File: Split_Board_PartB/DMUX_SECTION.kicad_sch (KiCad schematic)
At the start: 32 parts, among them J2 Conn_01x28, J3 Conn_01x28, U22 CD74HC4051PWT, U25 OPA187IDBVR, U30 CD74HC595SM96

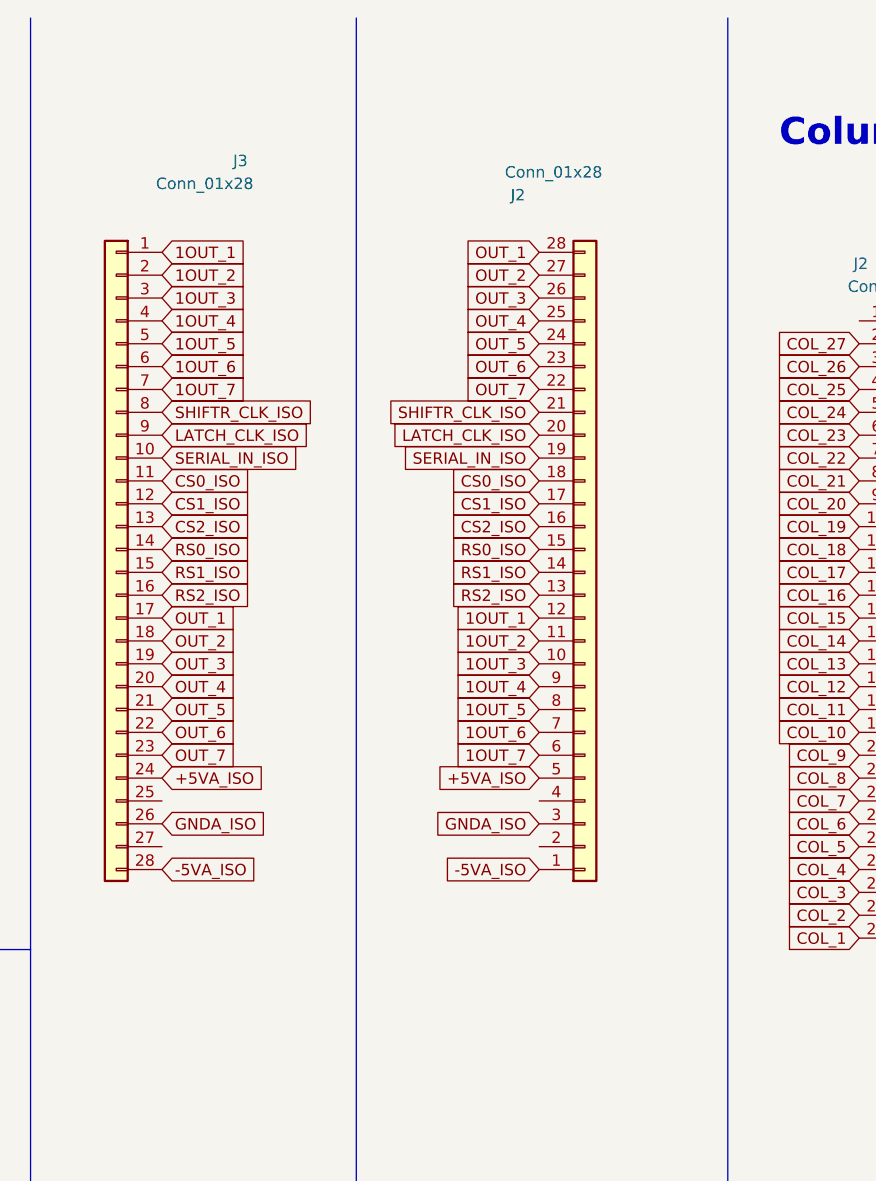
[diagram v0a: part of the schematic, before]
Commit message: led indicator added in part B
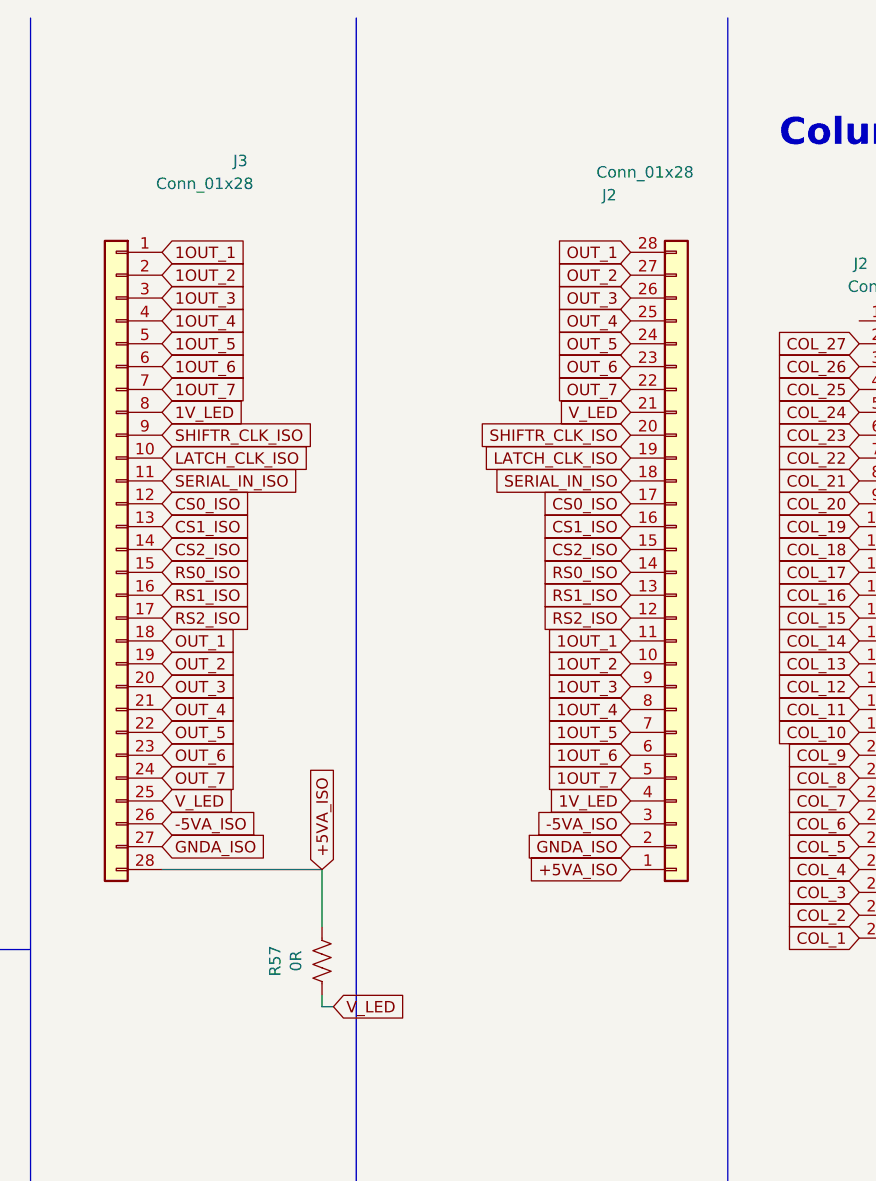
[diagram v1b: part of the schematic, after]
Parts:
- added R57: 0R, Resistor_SMD:R_0805_2012Metric_Pad1.20x1.40mm_HandSolder, symbol Device:R_US
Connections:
- net +5VA_ISO: now also J2.1 (Pin_1), J3.28 (Pin_28), R57.1; no longer J2.5 (Pin_5), J3.24 (Pin_24)
- net -5VA_ISO: now also J2.3 (Pin_3), J3.26 (Pin_26); no longer J2.1 (Pin_1), J3.28 (Pin_28)
- net 1OUT_1: now also J2.11 (Pin_11); no longer J2.12 (Pin_12)
- net 1OUT_2: now also J2.10 (Pin_10); no longer J2.11 (Pin_11)
- net 1OUT_3: now also J2.9 (Pin_9); no longer J2.10 (Pin_10)
- net 1OUT_4: now also J2.8 (Pin_8); no longer J2.9 (Pin_9)
- net 1OUT_5: now also J2.7 (Pin_7); no longer J2.8 (Pin_8)
- net 1OUT_6: now also J2.6 (Pin_6); no longer J2.7 (Pin_7)
- net 1OUT_7: now also J2.5 (Pin_5); no longer J2.6 (Pin_6)
- net CS0_ISO: now also J2.17 (Pin_17), J3.12 (Pin_12); no longer J2.18 (Pin_18), J3.11 (Pin_11)
- net CS1_ISO: now also J2.16 (Pin_16), J3.13 (Pin_13); no longer J2.17 (Pin_17), J3.12 (Pin_12)
- net CS2_ISO: now also J2.15 (Pin_15), J3.14 (Pin_14); no longer J2.16 (Pin_16), J3.13 (Pin_13)
- net GNDA: now also J2.2 (Pin_2), J3.27 (Pin_27); no longer J2.3 (Pin_3), J3.26 (Pin_26)
- net LATCH_CLK_ISO: now also J2.19 (Pin_19), J3.10 (Pin_10); no longer J2.20 (Pin_20), J3.9 (Pin_9)
- net OUT_1: now also J3.18 (Pin_18); no longer J3.17 (Pin_17)
- net OUT_2: now also J3.19 (Pin_19); no longer J3.18 (Pin_18)
- net OUT_3: now also J3.20 (Pin_20); no longer J3.19 (Pin_19)
- net OUT_4: now also J3.21 (Pin_21); no longer J3.20 (Pin_20)
- net OUT_5: now also J3.22 (Pin_22); no longer J3.21 (Pin_21)
- net OUT_6: now also J3.23 (Pin_23); no longer J3.22 (Pin_22)
- net OUT_7: now also J3.24 (Pin_24); no longer J3.23 (Pin_23)
- net RS0_ISO: now also J2.14 (Pin_14), J3.15 (Pin_15); no longer J2.15 (Pin_15), J3.14 (Pin_14)
- net RS1_ISO: now also J2.13 (Pin_13), J3.16 (Pin_16); no longer J2.14 (Pin_14), J3.15 (Pin_15)
- net RS2_ISO: now also J2.12 (Pin_12), J3.17 (Pin_17); no longer J2.13 (Pin_13), J3.16 (Pin_16)
- net SERIAL_IN_ISO: now also J2.18 (Pin_18), J3.11 (Pin_11); no longer J2.19 (Pin_19), J3.10 (Pin_10)
- net SHIFTR_CLK_ISO: now also J2.20 (Pin_20), J3.9 (Pin_9); no longer J2.21 (Pin_21), J3.8 (Pin_8)
- net 1V_LED: now reaches J2.4 (Pin_4)
- net 1V_LED: now also J3.8 (Pin_8)
- net V_LED: now reaches J3.25 (Pin_25)
- net V_LED: now also J2.21 (Pin_21), R57.2
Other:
- moved on the sheet: J2

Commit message: Removed the gerber files of espv5.0
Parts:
- R57: value 0R -> 1K
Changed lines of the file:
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@@
     (stroke (width 0) (type default))
   )
-  (polyline (pts (xy 336.55 12.065) (xy 336.55 252.73))
+  (polyline (pts (xy 347.345 12.065) (xy 347.345 252.73))
     (stroke (width 0) (type default))
   )
@@
       (effects (font (size 1.27 1.27)))
     )
-    (property "Value" "0R" (at 329.8444 116.84 90)
+    (property "Value" "1K" (at 329.8444 116.84 90)
       (effects (font (size 1.27 1.27)))
     )

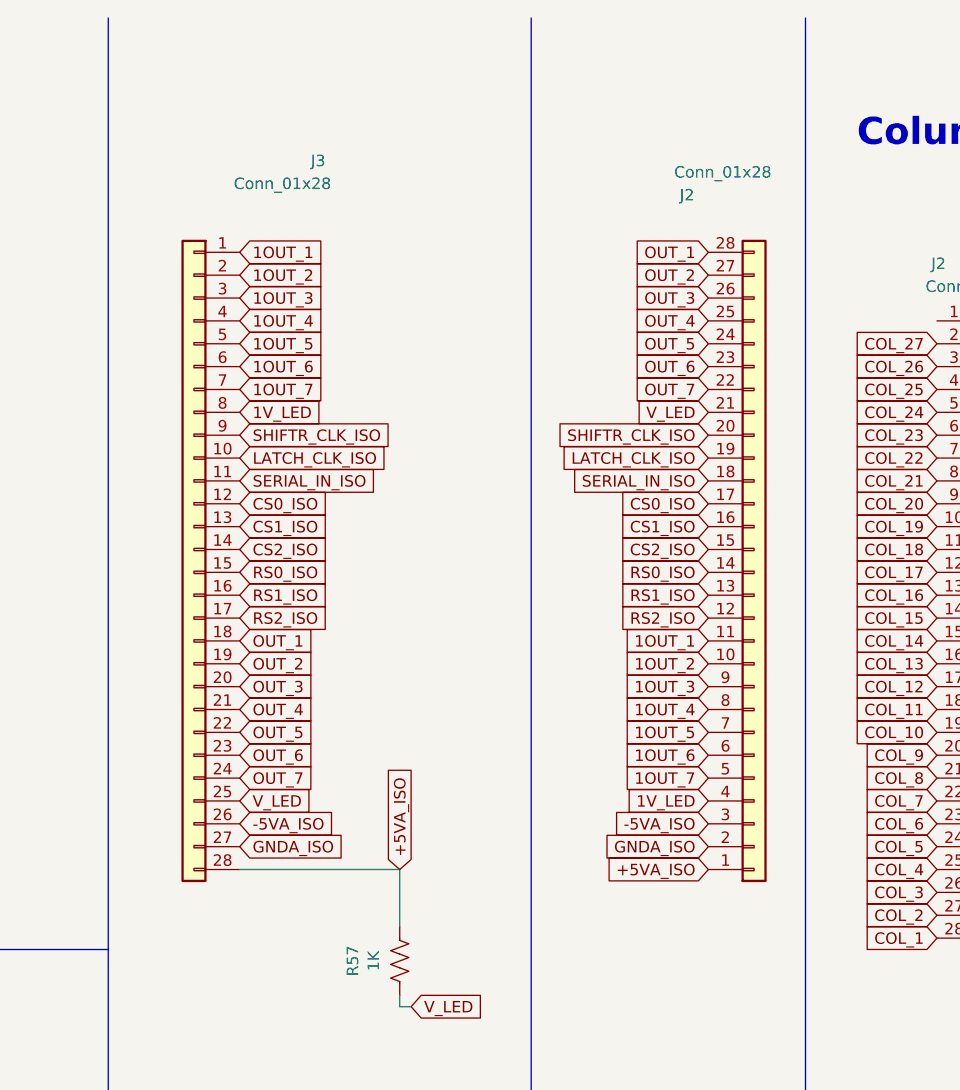
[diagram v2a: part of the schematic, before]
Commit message: added a adapter board in part b and edited the db37 connector in part A
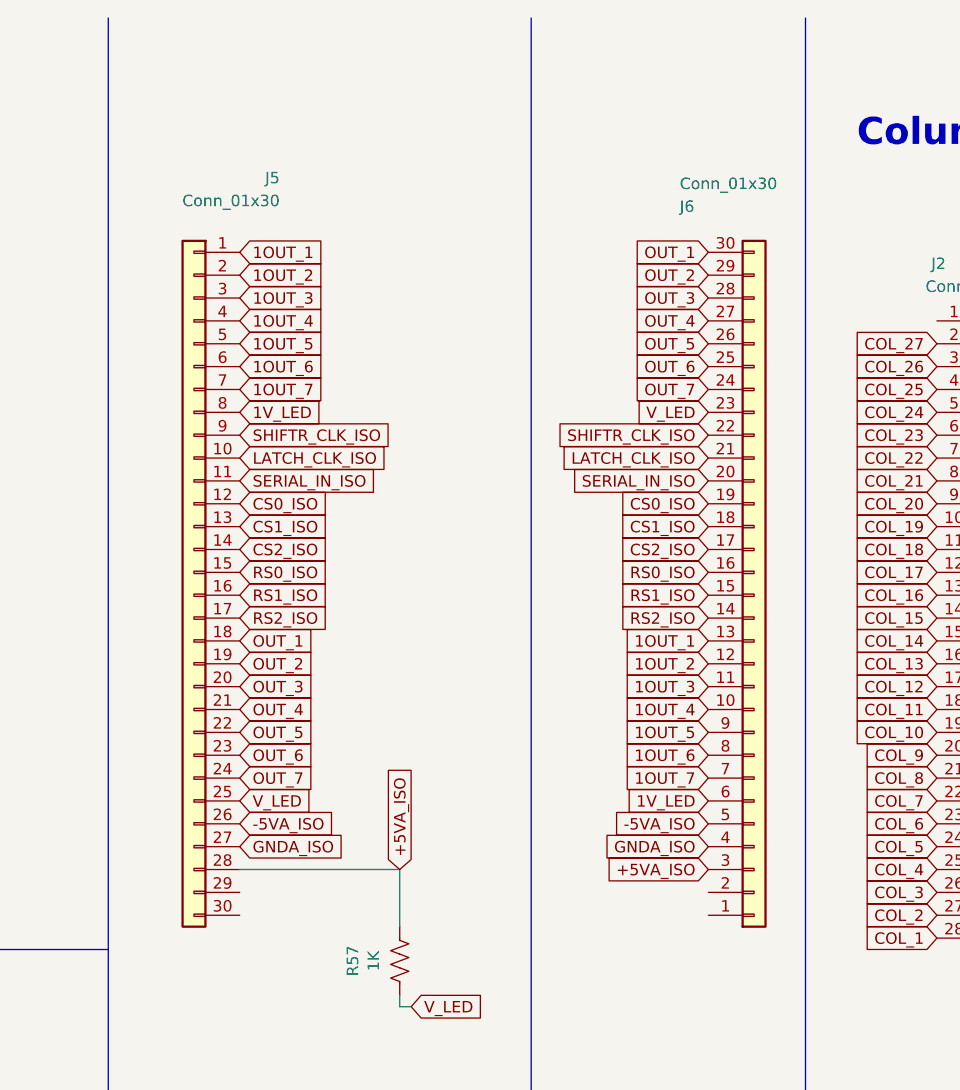
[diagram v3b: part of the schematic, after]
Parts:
- removed J2, J3: Conn_01x28, SamacSys_Parts:522072833, symbol Connector_Generic:Conn_01x28
- added J5, J6: Conn_01x30, symbol Connector_Generic:Conn_01x30
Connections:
- net +5VA_ISO: now also J5.28 (Pin_28), J6.3 (Pin_3)
- net -5VA_ISO: now also J5.26 (Pin_26), J6.5 (Pin_5)
- net 1OUT_1: now also J5.1 (Pin_1), J6.13 (Pin_13)
- net 1OUT_2: now also J5.2 (Pin_2), J6.12 (Pin_12)
- net 1OUT_3: now also J5.3 (Pin_3), J6.11 (Pin_11)
- net 1OUT_4: now also J5.4 (Pin_4), J6.10 (Pin_10)
- net 1OUT_5: now also J5.5 (Pin_5), J6.9 (Pin_9)
- net 1OUT_6: now also J5.6 (Pin_6), J6.8 (Pin_8)
- net 1OUT_7: now also J5.7 (Pin_7), J6.7 (Pin_7)
- net 1V_LED: now also J5.8 (Pin_8), J6.6 (Pin_6)
- net CS0_ISO: now also J5.12 (Pin_12), J6.19 (Pin_19)
- net CS1_ISO: now also J5.13 (Pin_13), J6.18 (Pin_18)
- net CS2_ISO: now also J5.14 (Pin_14), J6.17 (Pin_17)
- net GNDA: now also J5.27 (Pin_27), J6.4 (Pin_4)
- net LATCH_CLK_ISO: now also J5.10 (Pin_10), J6.21 (Pin_21)
- net OUT_1: now also J5.18 (Pin_18), J6.30 (Pin_30)
- net OUT_2: now also J5.19 (Pin_19), J6.29 (Pin_29)
- net OUT_3: now also J5.20 (Pin_20), J6.28 (Pin_28)
- net OUT_4: now also J5.21 (Pin_21), J6.27 (Pin_27)
- net OUT_5: now also J5.22 (Pin_22), J6.26 (Pin_26)
- net OUT_6: now also J5.23 (Pin_23), J6.25 (Pin_25)
- net OUT_7: now also J5.24 (Pin_24), J6.24 (Pin_24)
- net RS0_ISO: now also J5.15 (Pin_15), J6.16 (Pin_16)
- net RS1_ISO: now also J5.16 (Pin_16), J6.15 (Pin_15)
- net RS2_ISO: now also J5.17 (Pin_17), J6.14 (Pin_14)
- net SERIAL_IN_ISO: now also J5.11 (Pin_11), J6.20 (Pin_20)
- net SHIFTR_CLK_ISO: now also J5.9 (Pin_9), J6.22 (Pin_22)
- net V_LED: now also J5.25 (Pin_25), J6.23 (Pin_23)

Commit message: added a BOM and a final versions of all  the files schematic and design file
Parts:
- J5, J6: footprint (none) -> Connector_FFC-FPC:Hirose_FH12-30S-0.5SH_1x30-1MP_P0.50mm_Horizontal
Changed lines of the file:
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@@
       (effects (font (size 1.27 1.27)) (justify left))
     )
-    (property "Footprint" "" (at 372.11 76.2 0)
+    (property "Footprint" "Connector_FFC-FPC:Hirose_FH12-30S-0.5SH_1x30-1MP_P0.50mm_Horizontal" (at 372.11 76.2 0)
       (effects (font (size 1.27 1.27)) hide)
     )
@@
       (effects (font (size 1.27 1.27)) (justify left))
     )
-    (property "Footprint" "" (at 309.88 73.66 0)
+    (property "Footprint" "Connector_FFC-FPC:Hirose_FH12-30S-0.5SH_1x30-1MP_P0.50mm_Horizontal" (at 309.88 73.66 0)
       (effects (font (size 1.27 1.27)) hide)
     )
